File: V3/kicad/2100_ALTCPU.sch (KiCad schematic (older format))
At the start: 8 parts, among them J2100 Conn_02x24_Counter_Clockwise, J2101 Conn_01x02_Male, U2100 Z8-L180-S180-180-PQFP-80, U2101 GAL16V8, X2100 14.7456 MHz

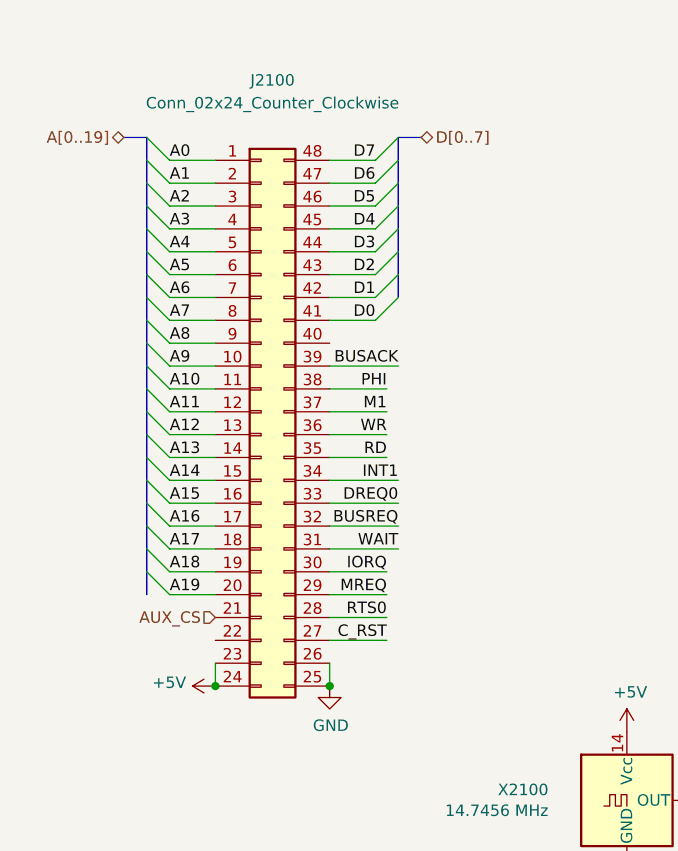
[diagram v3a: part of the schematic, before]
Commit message: new footprints and fixed reset routes
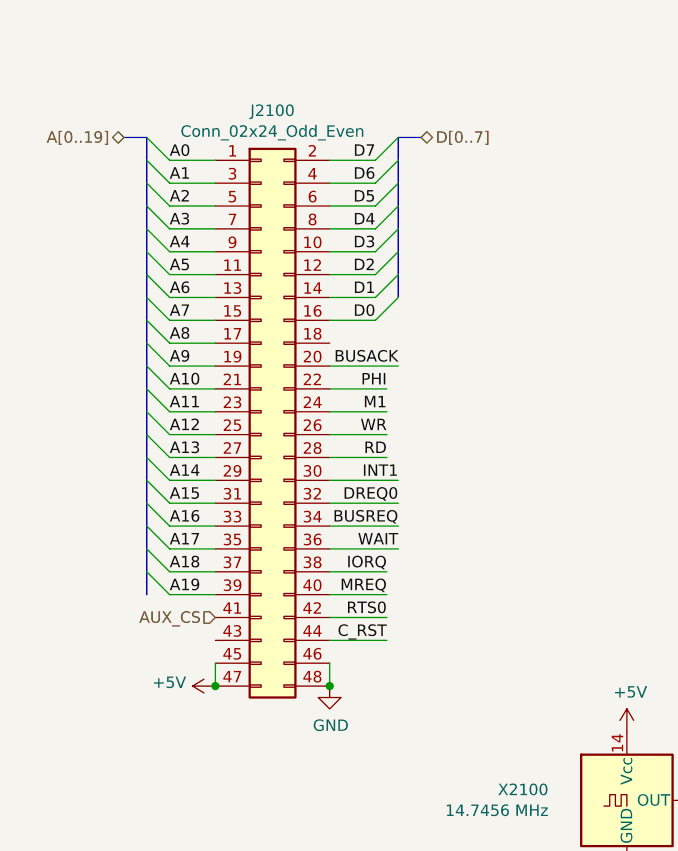
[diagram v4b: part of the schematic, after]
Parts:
- removed J2100: Conn_02x24_Counter_Clockwise, Connector_PinSocket_2.54mm:PinSocket_2x24_P2.54mm_Vertical, symbol Connector_Generic:Conn_02x24_Counter_Clockwise
- added J2100: Conn_02x24_Odd_Even, Connector_PinSocket_2.54mm:PinSocket_2x24_P2.54mm_Vertical, symbol Connector_Generic:Conn_02x24_Odd_Even
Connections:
- net +5V: now also J2100.45 (Pin_45), J2100.47 (Pin_47)
- net A0: now also J2100.1 (Pin_1)
- net A1: now also J2100.3 (Pin_3)
- net A10: now also J2100.21 (Pin_21)
- net A11: now also J2100.23 (Pin_23)
- net A12: now also J2100.25 (Pin_25)
- net A13: now also J2100.27 (Pin_27)
- net A14: now also J2100.29 (Pin_29)
- net A15: now also J2100.31 (Pin_31)
- net A16: now also J2100.33 (Pin_33)
- net A17: now also J2100.35 (Pin_35)
- net A18: now also J2100.37 (Pin_37)
- net A19: now also J2100.39 (Pin_39)
- net A2: now also J2100.5 (Pin_5)
- net A3: now also J2100.7 (Pin_7)
- net A4: now also J2100.9 (Pin_9)
- net A5: now also J2100.11 (Pin_11)
- net A6: now also J2100.13 (Pin_13)
- net A7: now also J2100.15 (Pin_15)
- net A8: now also J2100.17 (Pin_17)
- net A9: now also J2100.19 (Pin_19)
- net AUX_CS: now also J2100.41 (Pin_41)
- net BUSACK: now also J2100.20 (Pin_20)
- net BUSREQ: now also J2100.34 (Pin_34)
- net C_RST: now also J2100.44 (Pin_44)
- net D0: now also J2100.16 (Pin_16)
- net D1: now also J2100.14 (Pin_14)
- net D2: now also J2100.12 (Pin_12)
- net D3: now also J2100.10 (Pin_10)
- net D4: now also J2100.8 (Pin_8)
- net D5: now also J2100.6 (Pin_6)
- net D6: now also J2100.4 (Pin_4)
- net D7: now also J2100.2 (Pin_2)
- net DREQ0: now also J2100.32 (Pin_32)
- net GND: now also J2100.46 (Pin_46), J2100.48 (Pin_48)
- net INT1: now also J2100.30 (Pin_30)
- net IORQ: now also J2100.38 (Pin_38)
- net M1: now also J2100.24 (Pin_24)
- net MREQ: now also J2100.40 (Pin_40)
- net PHI: now also J2100.22 (Pin_22)
- net RD: now also J2100.28 (Pin_28)
- net RTS0: now also J2100.42 (Pin_42)
- net WAIT: now also J2100.36 (Pin_36)
- net WR: now also J2100.26 (Pin_26)
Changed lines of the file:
@@
 Wire Wire Line
 	9750 4150 9950 4150
-$Comp
-L Connector_Generic:Conn_02x24_Counter_Clockwise J2100
-U 1 1 62808857
-P 1800 2950
-F 0 "J2100" H 1850 4400 50  0000 C CNN
-F 1 "Conn_02x24_Counter_Clockwise" H 1850 4300 50  0000 C CNN
-F 2 "Connector_PinSocket_2.54mm:PinSocket_2x24_P2.54mm_Vertical" H 1800 2950 50  0001 C CNN
-F 3 "~" H 1800 2950 50  0001 C CNN
-	1    1800 2950
-	1    0    0    -1
-$EndComp
 Wire Wire Line
 	2100 3150 2350 3150
@@
 Wire Wire Line
 	2100 4150 2100 4050
-Connection ~ 2100 4150
 Wire Wire Line
 	1600 4150 1600 4050
-Connection ~ 1600 4150
 Wire Wire Line
 	6750 2300 7050 2300
@@
 Text Label 2400 2750 2    50   ~ 0
 BUSACK
+$Comp
+L Connector_Generic:Conn_02x24_Odd_Even J2100
+U 1 1 6294FC30
+P 1800 2950
+F 0 "J2100" H 1850 4267 50  0000 C CNN
+F 1 "Conn_02x24_Odd_Even" H 1850 4176 50  0000 C CNN
+F 2 "Connector_PinSocket_2.54mm:PinSocket_2x24_P2.54mm_Vertical" H 1800 2950 50  0001 C CNN
+F 3 "~" H 1800 2950 50  0001 C CNN
+	1    1800 2950
+	1    0    0    -1
+$EndComp
+Connection ~ 1600 4150
+Connection ~ 2100 4150
 Wire Bus Line
 	1600 6350 1600 6550

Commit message: last changes before autoroute
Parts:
- added C2100, C2101: 22pf, Capacitor_THT:C_Rect_L4.0mm_W2.5mm_P2.50mm, symbol Device:C
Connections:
- net +5V: now also C2100.1, C2101.1
- net GND: now also C2100.2, C2101.2
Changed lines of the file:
@@
 Connection ~ 1600 4150
 Connection ~ 2100 4150
+$Comp
+L Device:C C?
+U 1 1 62809F42
+P 8100 1650
+AR Path="/6195D2C9/62809F42" Ref="C?"  Part="1"
+AR Path="/6191B6A2/61F28B7D/62809F42" Ref="C?"  Part="1"
+AR Path="/6191B6A2/61EBDADB/62809F42" Ref="C2100"  Part="1"
+F 0 "C2100" H 8215 1696 50  0000 L CNN
+F 1 "22pf" H 8215 1605 50  0000 L CNN
+F 2 "Capacitor_THT:C_Rect_L4.0mm_W2.5mm_P2.50mm" H 8138 1500 50  0001 C CNN
+F 3 "~" H 8100 1650 50  0001 C CNN
+	1    8100 1650
+	1    0    0    -1
+$EndComp
+$Comp
+L power:GND #PWR?
+U 1 1 62809F48
+P 8100 1800
+AR Path="/62809F48" Ref="#PWR?"  Part="1"
+AR Path="/62497D60/62809F48" Ref="#PWR?"  Part="1"
+AR Path="/61D852D7/62809F48" Ref="#PWR?"  Part="1"
+AR Path="/6195D2C9/62809F48" Ref="#PWR?"  Part="1"
+AR Path="/6191B6A2/61F28B7D/62809F48" Ref="#PWR?"  Part="1"
+F 0 "#PWR?" H 8100 1550 50  0001 C CNN
+F 1 "GND" H 8105 1627 50  0000 C CNN
+F 2 "" H 8100 1800 50  0001 C CNN
+F 3 "" H 8100 1800 50  0001 C CNN
+	1    8100 1800
+	1    0    0    -1
+$EndComp
+$Comp
+L power:+5V #PWR?
+U 1 1 62809F4E
+P 8100 1500
+AR Path="/6195D2C9/62809F4E" Ref="#PWR?"  Part="1"
+AR Path="/6191B6A2/61F28B7D/62809F4E" Ref="#PWR?"  Part="1"
+F 0 "#PWR?" H 8100 1350 50  0001 C CNN
+F 1 "+5V" H 8115 1673 50  0000 C CNN
+F 2 "" H 8100 1500 50  0001 C CNN
+F 3 "" H 8100 1500 50  0001 C CNN
+	1    8100 1500
+	1    0    0    -1
+$EndComp
+$Comp
+L Device:C C?
+U 1 1 6281227F
+P 8700 1650
+AR Path="/6195D2C9/6281227F" Ref="C?"  Part="1"
+AR Path="/6191B6A2/61F28B7D/6281227F" Ref="C?"  Part="1"
+AR Path="/6191B6A2/61EBDADB/6281227F" Ref="C2101"  Part="1"
+F 0 "C2101" H 8815 1696 50  0000 L CNN
+F 1 "22pf" H 8815 1605 50  0000 L CNN
+F 2 "Capacitor_THT:C_Rect_L4.0mm_W2.5mm_P2.50mm" H 8738 1500 50  0001 C CNN
+F 3 "~" H 8700 1650 50  0001 C CNN
+	1    8700 1650
+	1    0    0    -1
+$EndComp
+$Comp
+L power:GND #PWR?
+U 1 1 62812285
+P 8700 1800
+AR Path="/62812285" Ref="#PWR?"  Part="1"
+AR Path="/62497D60/62812285" Ref="#PWR?"  Part="1"
+AR Path="/61D852D7/62812285" Ref="#PWR?"  Part="1"
+AR Path="/6195D2C9/62812285" Ref="#PWR?"  Part="1"
+AR Path="/6191B6A2/61F28B7D/62812285" Ref="#PWR?"  Part="1"
+F 0 "#PWR?" H 8700 1550 50  0001 C CNN
+F 1 "GND" H 8705 1627 50  0000 C CNN
+F 2 "" H 8700 1800 50  0001 C CNN
+F 3 "" H 8700 1800 50  0001 C CNN
+	1    8700 1800
+	1    0    0    -1
+$EndComp
+$Comp
+L power:+5V #PWR?
+U 1 1 6281228B
+P 8700 1500
+AR Path="/6195D2C9/6281228B" Ref="#PWR?"  Part="1"
+AR Path="/6191B6A2/61F28B7D/6281228B" Ref="#PWR?"  Part="1"
+F 0 "#PWR?" H 8700 1350 50  0001 C CNN
+F 1 "+5V" H 8715 1673 50  0000 C CNN
+F 2 "" H 8700 1500 50  0001 C CNN
+F 3 "" H 8700 1500 50  0001 C CNN
+	1    8700 1500
+	1    0    0    -1
+$EndComp
 Wire Bus Line
 	1600 6350 1600 6550

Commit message: still trying to make routes work
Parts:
- removed J2100: Conn_02x24_Odd_Even, Connector_PinSocket_2.54mm:PinSocket_2x24_P2.54mm_Vertical, symbol Connector_Generic:Conn_02x24_Odd_Even

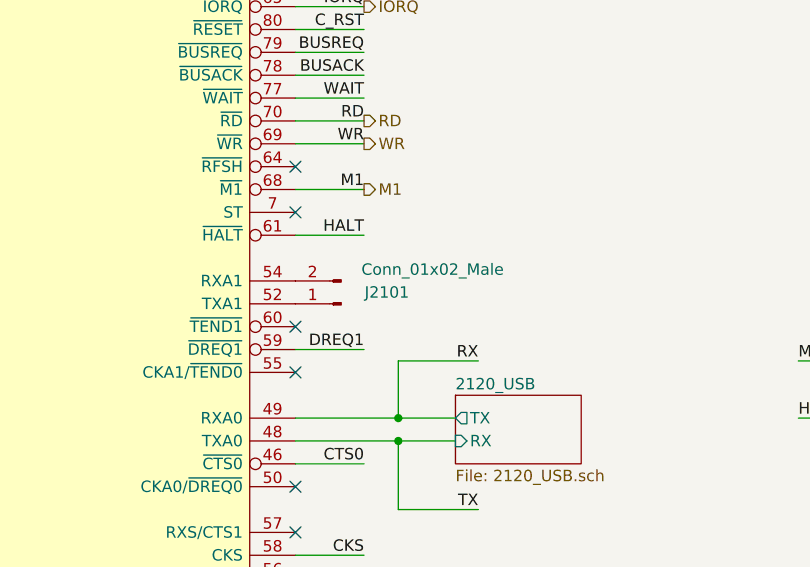
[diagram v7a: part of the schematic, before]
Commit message: more PIO routing
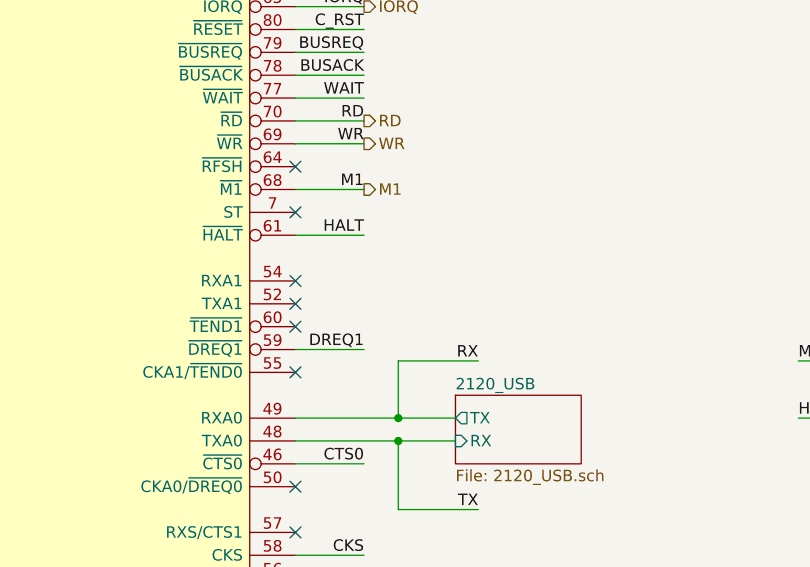
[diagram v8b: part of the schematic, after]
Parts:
- removed J2101: Conn_01x02_Male, Connector_PinHeader_2.54mm:PinHeader_1x02_P2.54mm_Vertical, symbol Connector:Conn_01x02_Male
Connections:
- no-connect marks 11 -> 13
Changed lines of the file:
@@
 Wire Wire Line
 	7200 4500 7200 4800
-$Comp
-L Connector:Conn_01x02_Male J?
-U 1 1 62765282
-P 6950 3900
-AR Path="/6191B6A2/61EBDADB/62542978/62765282" Ref="J?"  Part="1"
-AR Path="/6191B6A2/61EBDADB/62765282" Ref="J2101"  Part="1"
-F 0 "J2101" H 6750 3850 50  0000 C CNN
-F 1 "Conn_01x02_Male" H 6550 3750 50  0000 C CNN
-F 2 "Connector_PinHeader_2.54mm:PinHeader_1x02_P2.54mm_Vertical" H 6950 3900 50  0001 C CNN
-F 3 "~" H 6950 3900 50  0001 C CNN
-	1    6950 3900
-	-1   0    0    1
-$EndComp
 Wire Wire Line
 	9950 4300 10350 4300
@@
 Wire Bus Line
 	4300 3550 4200 3550
+NoConn ~ 6750 3800
+NoConn ~ 6750 3900
 Wire Bus Line
 	4300 3550 4300 4250
